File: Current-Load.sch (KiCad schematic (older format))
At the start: 6 parts, among them Q301 STP55NF06L, U201 MCP6002

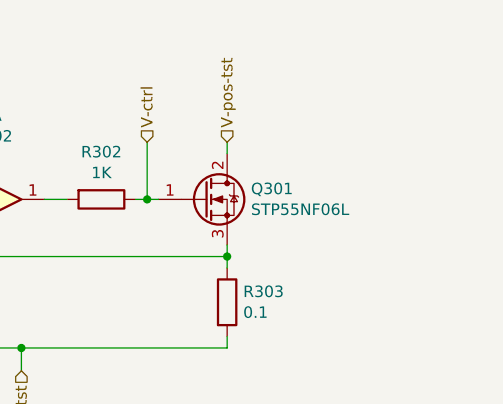
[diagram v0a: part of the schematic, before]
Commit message: Added heatsink to schematic and PCB
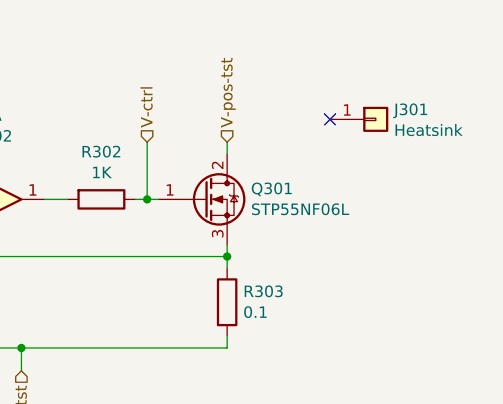
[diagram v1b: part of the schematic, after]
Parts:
- added J301: Heatsink, f:Heatsink, symbol Connector_Generic:Conn_01x01
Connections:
- no-connect marks 1 -> 2
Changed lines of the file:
@@
 V-neg-tst
 NoConn ~ 4650 3250
+$Comp
+L Connector_Generic:Conn_01x01 J301
+U 1 1 6021C92B
+P 7250 3000
+F 0 "J301" H 7330 3042 50  0000 L CNN
+F 1 "Heatsink" H 7330 2951 50  0000 L CNN
+F 2 "f:Heatsink" H 7250 3000 50  0001 C CNN
+F 3 "~" H 7250 3000 50  0001 C CNN
+	1    7250 3000
+	1    0    0    -1
+$EndComp
+NoConn ~ 7050 3000
 $EndSCHEMATC

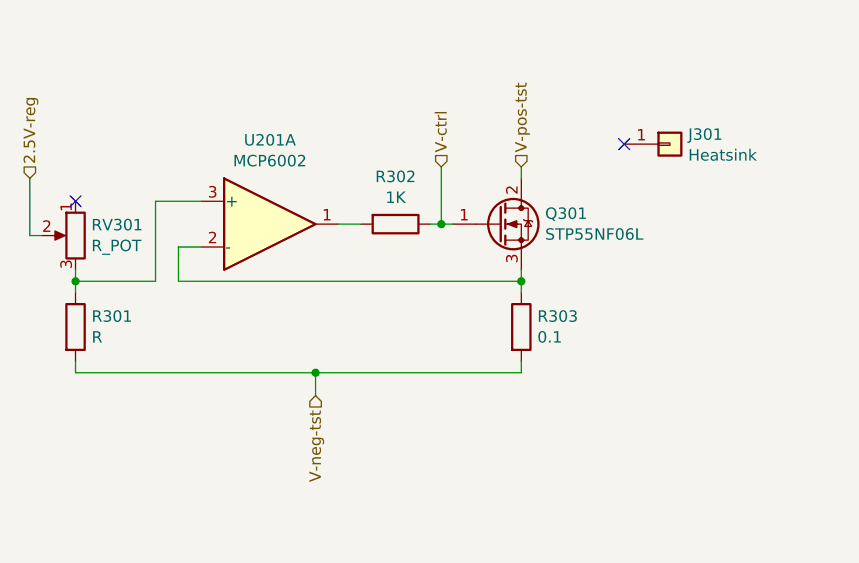
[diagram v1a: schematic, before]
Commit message: PCB completed with Op-Amp mounted horizontally
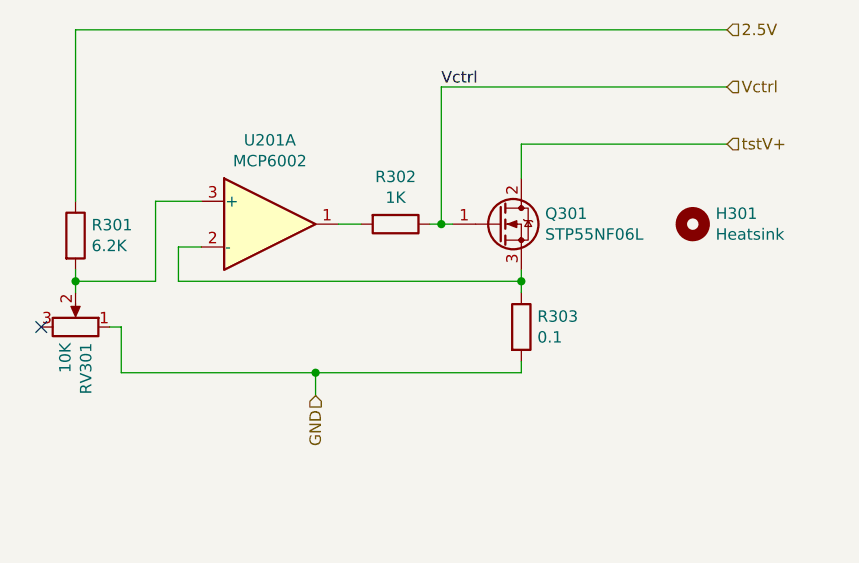
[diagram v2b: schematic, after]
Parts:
- removed J301: Heatsink, f:Heatsink, symbol Connector_Generic:Conn_01x01
- added H301: Heatsink, f:Heatsink, symbol Mechanical:MountingHole
- R301: value R -> 6.2K
- R303: MPN (none) -> CRA2512-FZ-R100ELF
- RV301: value R_POT -> 10K; footprint Potentiometer_THT:Potentiometer_Bourns_3266Y_Vertical -> f:POT_TTElect_P160KN; MPN (none) -> P160KN-0QD15B10K
- U201: footprint Package_SO:SOIC-8_3.9x4.9mm_P1.27mm -> (none); MPN MCP6002T-I/SN -> (none)
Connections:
- net GND: now reaches RV301.1
- net GND: now also R303.2
- net 2.5V-reg: no longer names the net of RV301.2
- net 2.5V-reg: now also R301.2, U201.3 (+)
- net V-ctrl renamed Vctrl
- removed net V-neg-tst: R301.2, R303.2
- net V-pos-tst renamed tstV+
- new net 2.5V: R301.1
- now unconnected: RV301.3
- no-connect marks 2 -> 1
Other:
- moved on the sheet: R301, RV301
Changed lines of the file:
@@
 $EndDescr
-$Comp
-L Amplifier_Operational:MCP6002-xSN U201
-U 1 1 6015D334
-P 5500 3350
-F 0 "U201" H 5500 3717 50  0000 C CNN
-F 1 "MCP6002" H 5500 3626 50  0000 C CNN
-F 2 "Package_SO:SOIC-8_3.9x4.9mm_P1.27mm" H 5500 3350 50  0001 C CNN
-F 3 "http://ww1.microchip.com/downloads/en/DeviceDoc/21733j.pdf" H 5500 3350 50  0001 C CNN
-F 4 "MCP6002T-I/SN" H 5500 3350 50  0001 C CNN "MPN"
-	1    5500 3350
-	1    0    0    -1
-$EndComp
 $Comp
 L Device:Q_NMOS_GDS Q?
@@
 F 1 "0.1" H 6670 3755 50  0000 L CNN
 F 2 "Resistor_SMD:R_2512_6332Metric_Pad1.40x3.35mm_HandSolder" V 6530 3800 50  0001 C CNN
-F 3 "~" H 6600 3800 50  0001 C CNN
+F 3 "https://www.bourns.com/docs/product-datasheets/cra.pdf" H 6600 3800 50  0001 C CNN
+F 4 "CRA2512-FZ-R100ELF" H 6600 3800 50  0001 C CNN "MPN"
 	1    6600 3800
-	1    0    0    -1
-$EndComp
-$Comp
-L Device:R R301
-U 1 1 6015D347
-P 4650 3800
-F 0 "R301" H 4720 3846 50  0000 L CNN
-F 1 "R" H 4720 3755 50  0000 L CNN
-F 2 "Resistor_SMD:R_0805_2012Metric_Pad1.20x1.40mm_HandSolder" V 4580 3800 50  0001 C CNN
-F 3 "~" H 4650 3800 50  0001 C CNN
-	1    4650 3800
 	1    0    0    -1
 $EndComp
@@
 	4650 3600 4650 3650
 Wire Wire Line
-	4650 3950 4650 4000
+	4850 3800 4850 4000
 Wire Wire Line
 	5800 3350 5900 3350
@@
 L Device:R_POT RV301
 U 1 1 6015D354
-P 4650 3400
-F 0 "RV301" H 4581 3446 50  0000 R CNN
-F 1 "R_POT" H 4581 3355 50  0000 R CNN
-F 2 "Potentiometer_THT:Potentiometer_Bourns_3266Y_Vertical" H 4650 3400 50  0001 C CNN
-F 3 "~" H 4650 3400 50  0001 C CNN
-	1    4650 3400
-	-1   0    0    -1
+P 4650 3800
+F 0 "RV301" H 4581 3846 50  0000 R CNN
+F 1 "10K" H 4581 3755 50  0000 R CNN
+F 2 "f:POT_TTElect_P160KN" H 4650 3800 50  0001 C CNN
+F 3 "https://www.ttelectronics.com/TTElectronics/media/ProductFiles/Potentiometers/Datasheets/P160.pdf" H 4650 3800 50  0001 C CNN
+F 4 "P160KN-0QD15B10K" H 4650 3800 50  0001 C CNN "MPN"
+	1    4650 3800
+	0    1    -1   0
 $EndComp
 Wire Wire Line
@@
 Wire Wire Line
 	6600 4000 5700 4000
-Connection ~ 5700 4000
-Wire Wire Line
-	5700 4000 4650 4000
 $Comp
 L Device:R R302
@@
 	5700 4100 5700 4000
 Wire Wire Line
-	4500 3400 4450 3400
-Wire Wire Line
-	4450 3150 4450 3400
-Wire Wire Line
 	4650 3550 4650 3600
 Connection ~ 4650 3600
@@
 Wire Wire Line
 	6200 3350 6250 3350
-Wire Wire Line
-	6600 3150 6600 3100
-Text HLabel 6250 3100 1    50   Input ~ 0
-V-ctrl
-Wire Wire Line
-	6250 3100 6250 3350
+Text HLabel 7500 2750 2    50   Input ~ 0
+Vctrl
 Connection ~ 6250 3350
 Wire Wire Line
 	6250 3350 6300 3350
-Text HLabel 6600 3100 1    50   Input ~ 0
-V-pos-tst
-Text HLabel 4450 3150 1    50   Input ~ 0
-2.5V-reg
+Text HLabel 7500 3000 2    50   Input ~ 0
+tstV+
+Text HLabel 7500 2500 2    50   Input ~ 0
+2.5V
 Text HLabel 5700 4100 3    50   Input ~ 0
-V-neg-tst
-NoConn ~ 4650 3250
+GND
+NoConn ~ 4500 3800
+Wire Wire Line
+	4800 3800 4850 3800
+Wire Wire Line
+	4850 4000 5700 4000
+Connection ~ 5700 4000
 $Comp
-L Connector_Generic:Conn_01x01 J301
-U 1 1 6021C92B
-P 7250 3000
-F 0 "J301" H 7330 3042 50  0000 L CNN
-F 1 "Heatsink" H 7330 2951 50  0000 L CNN
-F 2 "f:Heatsink" H 7250 3000 50  0001 C CNN
-F 3 "~" H 7250 3000 50  0001 C CNN
-	1    7250 3000
+L Device:R R301
+U 1 1 6015D347
+P 4650 3400
+F 0 "R301" H 4720 3446 50  0000 L CNN
+F 1 "6.2K" H 4720 3355 50  0000 L CNN
+F 2 "Resistor_SMD:R_0805_2012Metric_Pad1.20x1.40mm_HandSolder" V 4580 3400 50  0001 C CNN
+F 3 "~" H 4650 3400 50  0001 C CNN
+	1    4650 3400
 	1    0    0    -1
 $EndComp
-NoConn ~ 7050 3000
+$Comp
+L Mechanical:MountingHole H301
+U 1 1 6028E2EB
+P 7350 3350
+F 0 "H301" H 7450 3396 50  0000 L CNN
+F 1 "Heatsink" H 7450 3305 50  0000 L CNN
+F 2 "f:Heatsink" H 7350 3350 50  0001 C CNN
+F 3 "https://www.boydcorp.com/aavid-datasheets/Board-Level-Cooling-Extruded-5290.pdf" H 7350 3350 50  0001 C CNN
+F 4 "529802B02500G" H 7350 3350 50  0001 C CNN "MPN"
+	1    7350 3350
+	1    0    0    -1
+$EndComp
+Wire Wire Line
+	6600 3000 7500 3000
+Wire Wire Line
+	6600 3000 6600 3150
+Wire Wire Line
+	7500 2750 6250 2750
+Wire Wire Line
+	6250 2750 6250 3350
+Wire Wire Line
+	7500 2500 4650 2500
+Wire Wire Line
+	4650 2500 4650 3250
+Text Label 6250 2750 0    50   ~ 0
+Vctrl
+$Comp
+L Amplifier_Operational:MCP6002-xSN U201
+U 1 1 6039970D
+P 5500 3350
+F 0 "U201" H 5500 3717 50  0000 C CNN
+F 1 "MCP6002" H 5500 3626 50  0000 C CNN
+F 2 "" H 5500 3350 50  0001 C CNN
+F 3 "http://ww1.microchip.com/downloads/en/DeviceDoc/21733j.pdf" H 5500 3350 50  0001 C CNN
+	1    5500 3350
+	1    0    0    -1
+$EndComp
 $EndSCHEMATC

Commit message: Revision A as sent to OSHPark with some MPN updates due to availability
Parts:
- Q301: value STP55NF06L -> STP60NF06L; MPN STP55NF06L -> STP60NF06L
- R301, R302: footprint Resistor_SMD:R_0805_2012Metric_Pad1.20x1.40mm_HandSolder -> Resistor_SMD:R_0603_1608Metric_Pad0.98x0.95mm_HandSolder
- U201: footprint (none) -> Package_SO:SOIC-8_3.9x4.9mm_P1.27mm; MPN (none) -> MCP6002T-I/SN
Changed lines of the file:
@@
 AR Path="/601B7D0F/6015D33B" Ref="Q301"  Part="1"
 F 0 "Q301" H 6704 3396 50  0000 L CNN
-F 1 "STP55NF06L" H 6704 3305 50  0000 L CNN
+F 1 "STP60NF06L" H 6704 3305 50  0000 L CNN
 F 2 "Package_TO_SOT_THT:TO-220-3_Vertical" H 6700 3450 50  0001 C CNN
-F 3 "https://www.st.com/content/ccc/resource/technical/document/datasheet/49/c5/a8/71/93/60/4f/86/CD00002690.pdf/files/CD00002690.pdf/jcr:content/translations/en.CD00002690.pdf" H 6500 3350 50  0001 C CNN
-F 4 "STP55NF06L" H 6500 3350 50  0001 C CNN "MPN"
+F 3 "https://www.st.com/content/ccc/resource/technical/document/datasheet/57/fb/ac/00/b5/ba/4f/e7/CD00002907.pdf/files/CD00002907.pdf/jcr:content/translations/en.CD00002907.pdf" H 6500 3350 50  0001 C CNN
+F 4 "STP60NF06L" H 6500 3350 50  0001 C CNN "MPN"
 	1    6500 3350
 	1    0    0    -1
@@
 F 0 "R302" V 5843 3350 50  0000 C CNN
 F 1 "1K" V 5934 3350 50  0000 C CNN
-F 2 "Resistor_SMD:R_0805_2012Metric_Pad1.20x1.40mm_HandSolder" V 5980 3350 50  0001 C CNN
+F 2 "Resistor_SMD:R_0603_1608Metric_Pad0.98x0.95mm_HandSolder" V 5980 3350 50  0001 C CNN
 F 3 "~" H 6050 3350 50  0001 C CNN
 	1    6050 3350
@@
 F 0 "R301" H 4720 3446 50  0000 L CNN
 F 1 "6.2K" H 4720 3355 50  0000 L CNN
-F 2 "Resistor_SMD:R_0805_2012Metric_Pad1.20x1.40mm_HandSolder" V 4580 3400 50  0001 C CNN
+F 2 "Resistor_SMD:R_0603_1608Metric_Pad0.98x0.95mm_HandSolder" V 4580 3400 50  0001 C CNN
 F 3 "~" H 4650 3400 50  0001 C CNN
 	1    4650 3400
@@
 F 0 "U201" H 5500 3717 50  0000 C CNN
 F 1 "MCP6002" H 5500 3626 50  0000 C CNN
-F 2 "" H 5500 3350 50  0001 C CNN
+F 2 "Package_SO:SOIC-8_3.9x4.9mm_P1.27mm" H 5500 3350 50  0001 C CNN
 F 3 "http://ww1.microchip.com/downloads/en/DeviceDoc/21733j.pdf" H 5500 3350 50  0001 C CNN
+F 4 "MCP6002T-I/SN" H 5500 3350 50  0001 C CNN "MPN"
 	1    5500 3350
 	1    0    0    -1

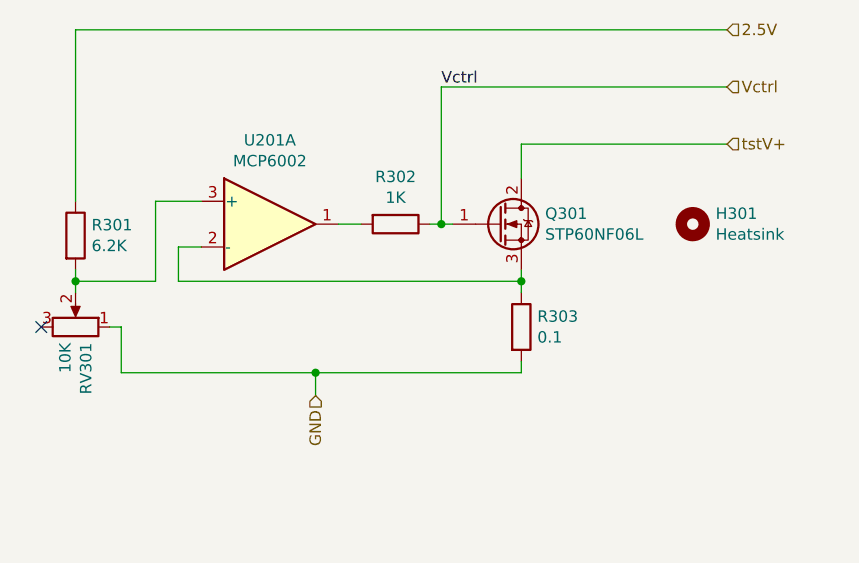
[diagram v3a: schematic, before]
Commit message: Fixed reversed Op-Amp for voltage limiting and potentiometer connections to allow for full range of the potentiometer.
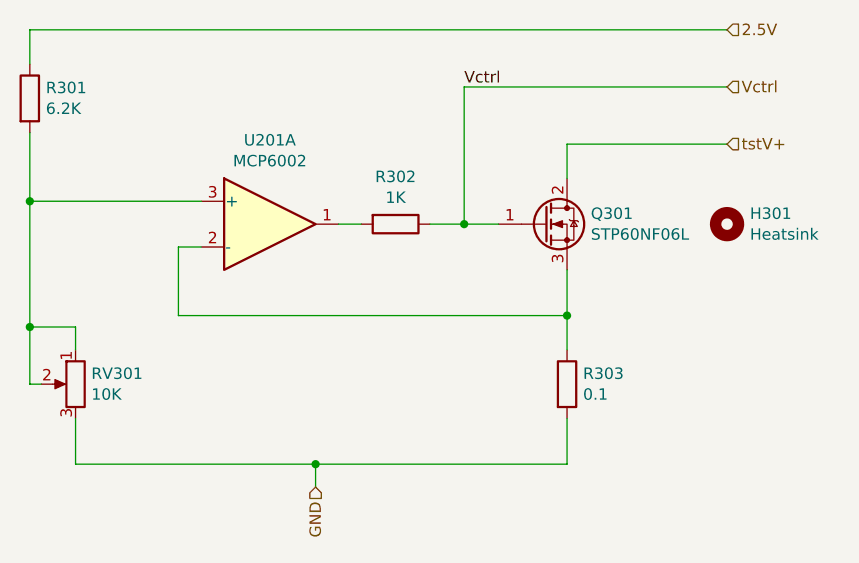
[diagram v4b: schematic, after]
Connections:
- net GND: now also RV301.3; no longer RV301.1
- net at R301.2, RV301.2, U201.3 (+): now also RV301.1
- no-connect marks 1 -> 0
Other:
- moved on the sheet: H301, Q301, R301, R303, RV301
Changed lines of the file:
@@
 L Device:Q_NMOS_GDS Q?
 U 1 1 6015D33B
-P 6500 3350
+P 6700 3350
 AR Path="/6015D33B" Ref="Q?"  Part="1"
 AR Path="/601B7D0F/6015D33B" Ref="Q301"  Part="1"
-F 0 "Q301" H 6704 3396 50  0000 L CNN
-F 1 "STP60NF06L" H 6704 3305 50  0000 L CNN
-F 2 "Package_TO_SOT_THT:TO-220-3_Vertical" H 6700 3450 50  0001 C CNN
-F 3 "https://www.st.com/content/ccc/resource/technical/document/datasheet/57/fb/ac/00/b5/ba/4f/e7/CD00002907.pdf/files/CD00002907.pdf/jcr:content/translations/en.CD00002907.pdf" H 6500 3350 50  0001 C CNN
-F 4 "STP60NF06L" H 6500 3350 50  0001 C CNN "MPN"
-	1    6500 3350
+F 0 "Q301" H 6904 3396 50  0000 L CNN
+F 1 "STP60NF06L" H 6904 3305 50  0000 L CNN
+F 2 "Package_TO_SOT_THT:TO-220-3_Vertical" H 6900 3450 50  0001 C CNN
+F 3 "https://www.st.com/content/ccc/resource/technical/document/datasheet/57/fb/ac/00/b5/ba/4f/e7/CD00002907.pdf/files/CD00002907.pdf/jcr:content/translations/en.CD00002907.pdf" H 6700 3350 50  0001 C CNN
+F 4 "STP60NF06L" H 6700 3350 50  0001 C CNN "MPN"
+	1    6700 3350
 	1    0    0    -1
 $EndComp
@@
 L Device:R R?
 U 1 1 6015D341
-P 6600 3800
+P 6800 4050
 AR Path="/6015D341" Ref="R?"  Part="1"
 AR Path="/601B7D0F/6015D341" Ref="R303"  Part="1"
-F 0 "R303" H 6670 3846 50  0000 L CNN
-F 1 "0.1" H 6670 3755 50  0000 L CNN
-F 2 "Resistor_SMD:R_2512_6332Metric_Pad1.40x3.35mm_HandSolder" V 6530 3800 50  0001 C CNN
-F 3 "https://www.bourns.com/docs/product-datasheets/cra.pdf" H 6600 3800 50  0001 C CNN
-F 4 "CRA2512-FZ-R100ELF" H 6600 3800 50  0001 C CNN "MPN"
-	1    6600 3800
+F 0 "R303" H 6870 4096 50  0000 L CNN
+F 1 "0.1" H 6870 4005 50  0000 L CNN
+F 2 "Resistor_SMD:R_2512_6332Metric_Pad1.40x3.35mm_HandSolder" V 6730 4050 50  0001 C CNN
+F 3 "https://www.bourns.com/docs/product-datasheets/cra.pdf" H 6800 4050 50  0001 C CNN
+F 4 "CRA2512-FZ-R100ELF" H 6800 4050 50  0001 C CNN "MPN"
+	1    6800 4050
 	1    0    0    -1
 $EndComp
 Wire Wire Line
-	5200 3250 5000 3250
-Wire Wire Line
-	5000 3250 5000 3600
-Wire Wire Line
-	5000 3600 4650 3600
-Wire Wire Line
-	4650 3600 4650 3650
-Wire Wire Line
-	4850 3800 4850 4000
-Wire Wire Line
 	5800 3350 5900 3350
 Wire Wire Line
-	6600 3550 6600 3600
+	6800 3550 6800 3750
 $Comp
 L Device:R_POT RV301
 U 1 1 6015D354
-P 4650 3800
-F 0 "RV301" H 4581 3846 50  0000 R CNN
-F 1 "10K" H 4581 3755 50  0000 R CNN
-F 2 "f:POT_TTElect_P160KN" H 4650 3800 50  0001 C CNN
-F 3 "https://www.ttelectronics.com/TTElectronics/media/ProductFiles/Potentiometers/Datasheets/P160.pdf" H 4650 3800 50  0001 C CNN
-F 4 "P160KN-0QD15B10K" H 4650 3800 50  0001 C CNN "MPN"
-	1    4650 3800
-	0    1    -1   0
+P 4650 4050
+F 0 "RV301" H 4581 4096 50  0000 R CNN
+F 1 "10K" H 4581 4005 50  0000 R CNN
+F 2 "f:POT_TTElect_P160KN" H 4650 4050 50  0001 C CNN
+F 3 "https://www.ttelectronics.com/TTElectronics/media/ProductFiles/Potentiometers/Datasheets/P160.pdf" H 4650 4050 50  0001 C CNN
+F 4 "P160KN-0QD15B10K" H 4650 4050 50  0001 C CNN "MPN"
+	1    4650 4050
+	-1   0    0    -1
 $EndComp
 Wire Wire Line
 	5200 3450 5100 3450
 Wire Wire Line
-	5100 3450 5100 3600
-Connection ~ 6600 3600
+	5100 3450 5100 3750
+Connection ~ 6800 3750
 Wire Wire Line
-	6600 3600 6600 3650
+	6800 3750 6800 3900
 Wire Wire Line
-	6600 3950 6600 4000
+	6800 4200 6800 4400
 Wire Wire Line
-	6600 4000 5700 4000
+	6800 4400 5700 4400
 $Comp
 L Device:R R302
@@
 $EndComp
 Wire Wire Line
-	5700 4100 5700 4000
+	5700 4500 5700 4400
 Wire Wire Line
-	4650 3550 4650 3600
-Connection ~ 4650 3600
+	5100 3750 6800 3750
 Wire Wire Line
-	5100 3600 6600 3600
-Wire Wire Line
-	6200 3350 6250 3350
+	6200 3350 6350 3350
 Text HLabel 7500 2750 2    50   Input ~ 0
 Vctrl
-Connection ~ 6250 3350
+Connection ~ 6350 3350
 Wire Wire Line
-	6250 3350 6300 3350
+	6350 3350 6500 3350
 Text HLabel 7500 3000 2    50   Input ~ 0
 tstV+
 Text HLabel 7500 2500 2    50   Input ~ 0
 2.5V
-Text HLabel 5700 4100 3    50   Input ~ 0
+Text HLabel 5700 4500 3    50   Input ~ 0
 GND
-NoConn ~ 4500 3800
-Wire Wire Line
-	4800 3800 4850 3800
-Wire Wire Line
-	4850 4000 5700 4000
-Connection ~ 5700 4000
+Connection ~ 5700 4400
 $Comp
 L Device:R R301
 U 1 1 6015D347
-P 4650 3400
-F 0 "R301" H 4720 3446 50  0000 L CNN
-F 1 "6.2K" H 4720 3355 50  0000 L CNN
-F 2 "Resistor_SMD:R_0603_1608Metric_Pad0.98x0.95mm_HandSolder" V 4580 3400 50  0001 C CNN
-F 3 "~" H 4650 3400 50  0001 C CNN
-	1    4650 3400
+P 4450 2800
+F 0 "R301" H 4520 2846 50  0000 L CNN
+F 1 "6.2K" H 4520 2755 50  0000 L CNN
+F 2 "Resistor_SMD:R_0603_1608Metric_Pad0.98x0.95mm_HandSolder" V 4380 2800 50  0001 C CNN
+F 3 "~" H 4450 2800 50  0001 C CNN
+	1    4450 2800
 	1    0    0    -1
 $EndComp
@@
 L Mechanical:MountingHole H301
 U 1 1 6028E2EB
-P 7350 3350
-F 0 "H301" H 7450 3396 50  0000 L CNN
-F 1 "Heatsink" H 7450 3305 50  0000 L CNN
-F 2 "f:Heatsink" H 7350 3350 50  0001 C CNN
-F 3 "https://www.boydcorp.com/aavid-datasheets/Board-Level-Cooling-Extruded-5290.pdf" H 7350 3350 50  0001 C CNN
-F 4 "529802B02500G" H 7350 3350 50  0001 C CNN "MPN"
-	1    7350 3350
+P 7500 3350
+F 0 "H301" H 7600 3396 50  0000 L CNN
+F 1 "Heatsink" H 7600 3305 50  0000 L CNN
+F 2 "f:Heatsink" H 7500 3350 50  0001 C CNN
+F 3 "https://www.boydcorp.com/aavid-datasheets/Board-Level-Cooling-Extruded-5290.pdf" H 7500 3350 50  0001 C CNN
+F 4 "529802B02500G" H 7500 3350 50  0001 C CNN "MPN"
+	1    7500 3350
 	1    0    0    -1
 $EndComp
 Wire Wire Line
-	6600 3000 7500 3000
+	6800 3000 7500 3000
 Wire Wire Line
-	6600 3000 6600 3150
+	6800 3000 6800 3150
 Wire Wire Line
-	7500 2750 6250 2750
+	7500 2750 6350 2750
 Wire Wire Line
-	6250 2750 6250 3350
+	6350 2750 6350 3350
 Wire Wire Line
-	7500 2500 4650 2500
+	7500 2500 4450 2500
 Wire Wire Line
-	4650 2500 4650 3250
-Text Label 6250 2750 0    50   ~ 0
+	4450 2500 4450 2650
+Text Label 6350 2750 0    50   ~ 0
 Vctrl
 $Comp
@@
 	1    0    0    -1
 $EndComp
+Wire Wire Line
+	4450 2950 4450 3250
+Wire Wire Line
+	4450 4050 4500 4050
+Wire Wire Line
+	4650 3900 4650 3800
+Wire Wire Line
+	4650 3800 4450 3800
+Connection ~ 4450 3800
+Wire Wire Line
+	4450 3800 4450 4050
+Wire Wire Line
+	4450 3250 5200 3250
+Connection ~ 4450 3250
+Wire Wire Line
+	4450 3250 4450 3800
+Wire Wire Line
+	4650 4200 4650 4400
+Wire Wire Line
+	4650 4400 5700 4400
 $EndSCHEMATC
